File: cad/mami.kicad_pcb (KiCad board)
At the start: 2 copper layers, 258.4 x 86.7 mm, 128 parts, among them SW1 SW_Push, SW10 SW_Push, SW11 SW_Push, SW12 SW_Push, SW13 SW_Push, SW14 SW_Push, SW15 SW_Push, SW16 SW_Push, SW17 SW_Push, SW18 SW_Push, SW19 SW_Push, SW2 SW_Push, SW20 SW_Push, SW21 SW_Push, SW22 SW_Push, SW23 SW_Push, SW24 SW_Push, SW25 SW_Push, SW26 SW_Push, SW27 SW_Push, SW28 SW_Push, SW29 SW_Push, SW3 SW_Push, SW30 SW_Push, SW31 SW_Push, SW32 SW_Push, SW33 SW_Push, SW34 SW_Push, SW35 SW_Push, SW36 SW_Push, SW37 SW_Push, SW38 SW_Push, SW39 SW_Push, SW4 SW_Push, SW40 SW_Push, SW41 SW_Push, SW42 SW_Push, SW43 ResetSW, SW5 SW_Push, SW6 SW_Push, SW7 SW_Push, SW8 SW_Push, SW9 SW_Push

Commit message: ON/OFFスイッチを削除
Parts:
- removed REF**: SuperMini, taku:nano
- added U1: nice_nano, salicylic-3:Micon_KMC_7sKB, F.Cu at (150.2, 62.9)
- moved D77 244.7 mm to (265.2, 100.0)
- moved D78 243.8 mm to (269.4, 80.9)
- moved D79 237.6 mm to (267.3, 61.9)
- moved D76 227.9 mm to (246.2, 99.9)
- moved D66 227.5 mm to (228.6, 118.4), turned to 8 degrees
- moved D75 225.8 mm to (248.1, 80.9)
- moved D80 217.8 mm to (248.1, 62.0)
- moved D67 216.4 mm to (225.9, 99.4), turned to 8 degrees
- moved D65 211.9 mm to (207.4, 121.2), turned to 8 degrees
- moved D74 207.5 mm to (228.1, 79.9), turned to 8 degrees
- moved D68 197.8 mm to (207.0, 102.1), turned to 8 degrees
- moved D81 196.2 mm to (227.4, 60.9), turned to 8 degrees
- moved D73 191.9 mm to (209.2, 82.5), turned to 8 degrees
- moved D64 190.5 mm to (176.8, 125.5), turned to 8 degrees
- moved D69 179.3 mm to (188.1, 104.7), turned to 8 degrees
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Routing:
- net col5: track 3.03 -> 0.49 mm, vias 3 -> 2
- net VCC: track 1.99 -> 0.00 mm, vias 1 -> 0
- net GND: track 1.41 -> 0.00 mm
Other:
- board size 258.4 x 86.7 mm -> 258.4 x 87.9 mm

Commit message: reverse diode direction
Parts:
- SW1, SW10, SW11, SW12, SW13, SW15, SW16, SW17, SW18, SW19, SW2, SW20, SW22, SW23, SW24, SW26, SW27, SW28, SW29, SW3, SW30, SW31, SW33, SW34, SW35, SW36, SW37, SW38, SW39, SW4, SW40, SW41, SW42, SW5, SW6, SW7, SW8, SW9: footprint kbd:keyswitch_cherrymx_hotswap_1u -> kbd-sw:CherryMX_Hotswap_1u
- SW14, SW32: footprint kbd:keyswitch_cherrymx_hotswap_1u -> kbd-sw:CherryMX_Hotswap_1.25u
- SW21, SW25: footprint kbd:keyswitch_cherrymx_hotswap_1u -> kbd-sw:CherryMX_Hotswap_2u
- U1: value nice_nano -> Micon_BLEMicroPro; footprint salicylic-3:Micon_KMC_7sKB -> kbd-parts:Micon_BMP_7sKB; moved to B.Cu
- moved D14 14.9 mm to (101.9, 123.9), turned to 82 degrees
- moved D40 14.7 mm to (274.6, 63.3), turned to 90 degrees
- moved D27 14.7 mm to (197.8, 85.5), turned to 98 degrees
- moved D30 14.6 mm to (216.7, 82.7), turned to 98 degrees
- moved D22 14.6 mm to (178.4, 69.1), turned to 98 degrees
- moved D32 14.5 mm to (215.1, 121.3), turned to 98 degrees
- moved D33 14.5 mm to (234.8, 61.1), turned to 98 degrees
- moved D29 14.5 mm to (216.1, 63.8), turned to 98 degrees
- moved D39 14.5 mm to (253.4, 101.3), turned to 90 degrees
- moved D13 14.5 mm to (100.4, 104.4), turned to 82 degrees
- moved D25 14.5 mm to (184.0, 125.9), turned to 98 degrees
- moved D21 14.5 mm to (131.1, 127.7), turned to 82 degrees
- moved D20 14.5 mm to (138.2, 109.7), turned to 82 degrees
- moved D9 14.5 mm to (81.8, 101.8), turned to 82 degrees
- moved D26 14.5 mm to (197.1, 66.3), turned to 98 degrees
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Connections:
- U1 pad 25: (no net) -> BAT+
- U1 pad 26: (no net) -> GND
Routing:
- net row0: track 1.27 -> 0.00 mm
- net Net-(D15-A): track 0.00 -> 1.27 mm
- net col5: track 0.49 -> 0.00 mm, vias 2 -> 0

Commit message: pcb枠を修正
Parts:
- moved SW43 18.9 mm to (150.1, 64.8)
- moved U1 10.8 mm to (150.2, 74.3)
- moved SW2 2.45 mm to (33.3, 76.2)
- moved D2 2.45 mm to (40.9, 81.8)
- moved D49 2.45 mm to (33.3, 80.9)
- moved D78 2.27 mm to (267.2, 81.0)
- moved D41 2.27 mm to (274.4, 82.1)
- moved SW41 2.27 mm to (267.2, 76.2)
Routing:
- net Net-(D15-A): track 1.27 -> 0.00 mm
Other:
- board size 258.4 x 87.9 mm -> 253.1 x 87.4 mm

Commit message: 自動配線
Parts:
- added J1: Conn_01x02_Pin, kbd-parts:Battery_BMP_2pin, B.Cu at (161.6, 70.2)
- SW43: moved to B.Cu
- moved SW43 28.6 mm to (122.8, 73.2), turned to -8 degrees
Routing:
- net VCC: track 0.00 -> 1027.1 mm, vias 0 -> 82
- net GND: track 0.00 -> 1018.7 mm, vias 0 -> 72
- net col0: track 0.00 -> 342.0 mm, vias 0 -> 9
- net col1: track 0.00 -> 286.1 mm, vias 0 -> 8
- net col2: track 0.00 -> 283.6 mm, vias 0 -> 6
- net col3: track 0.00 -> 241.2 mm, vias 0 -> 5
- net col4: track 0.00 -> 166.0 mm, vias 0 -> 2
- net col5: track 0.00 -> 163.4 mm, vias 0 -> 3
- net row6: track 0.00 -> 140.6 mm, vias 0 -> 4
- net row2: track 0.00 -> 135.8 mm, vias 0 -> 3
- net row4: track 0.00 -> 133.4 mm, vias 0 -> 9
- net row5: track 0.00 -> 128.2 mm, vias 0 -> 3
- net row7: track 0.00 -> 123.8 mm, vias 0 -> 5
- net row0: track 0.00 -> 117.0 mm, vias 0 -> 9
- net row1: track 0.00 -> 116.5 mm, vias 0 -> 1
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
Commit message: routing width > 0.250mm
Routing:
- net GND: track 1018.7 -> 994.8 mm, vias 72 -> 67
- net col4: track 166.0 -> 181.6 mm, vias 2 -> 7
- net Net-(D60-DOUT): track 30.6 -> 44.1 mm, vias 2 -> 6
- net Net-(D83-DOUT): track 28.6 -> 41.3 mm, vias 2 -> 4
- net Net-(D49-DOUT): track 22.8 -> 35.2 mm, vias 2 -> 4
- net Net-(D46-DOUT): track 30.8 -> 40.9 mm, vias 2 -> 4
- net Net-(D75-DOUT): track 28.5 -> 37.6 mm, vias 2 -> 4
- net VCC: track 1027.1 -> 1018.2 mm, vias 82 -> 81
- net col3: track 241.2 -> 249.5 mm
- net Net-(D44-DOUT): track 34.1 -> 42.3 mm, vias 2 -> 4
- net Net-(D57-DOUT): track 50.3 -> 42.2 mm, vias 6 -> 4
- net col0: track 342.0 -> 334.6 mm, vias 9 -> 3
- net Net-(D43-DOUT): track 38.7 -> 45.5 mm
- net row4: track 133.4 -> 139.9 mm, vias 9 -> 11
- net Net-(D80-DOUT): track 47.0 -> 40.8 mm, vias 6 -> 4
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
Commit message: ラベリング
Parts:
- J1: moved to F.Cu
- turned J1 to 180 degrees
- renumbered SW5 to A, SW20 to B, SW39 to BLSH, SW40 to BSPC, SW13 to C, SW32 to CMD, SW14 to CMD, SW38 to COLON, SW31 to COMMA, SW10 to CTRL, SW12 to D, D83 to D41, SW35 to DOT, SW11 to E, SW1 to ECS, SW41 to ENTER, SW16 to F, SW19 to G, SW23 to H, SW29 to I, SW27 to J, SW30 to K, SW34 to L, D43 to L1, D52 to L10, D53 to L11, D54 to L12, D55 to L13, D56 to L14, D57 to L15, D58 to L16, D59 to L17, D60 to L18, D61 to L19, D44 to L2, D62 to L20, D63 to L21, D64 to L22, D65 to L23, D66 to L24, D67 to L25, D68 to L26, D69 to L27, D70 to L28, D71 to L29, D45 to L3, D72 to L30, D73 to L31, D74 to L32, D75 to L33, D76 to L34, D77 to L35, D78 to L36, D79 to L37, D80 to L38, D81 to L39, D46 to L4, D82 to L40, D84 to L42, D47 to L5, D48 to L6, D49 to L7, D50 to L8, D51 to L9, SW28 to M, SW24 to N, SW33 to O, SW36 to OPT, SW37 to P, SW4 to Q, SW15 to R, SW8 to S, SW3 to SHIFT, SW42 to SHIFT, SW25 to SPACE, SW21 to SPACE, SW18 to T, SW2 to TAB, SW26 to U, SW17 to V, SW7 to W, SW9 to X, SW22 to Y, SW6 to Z
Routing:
- net row7: track 117.8 -> 181.1 mm, vias 6 -> 4
- net VCC: track 1018.2 -> 1006.4 mm, vias 81 -> 91
- net col3: track 249.5 -> 261.1 mm, vias 5 -> 4
- net Net-(D57-DOUT): track 42.2 -> 33.0 mm, vias 4 -> 2
- net col2: track 282.9 -> 291.6 mm, vias 8 -> 10
- net Net-(D34-A): track 11.7 -> 20.1 mm, vias 1 -> 3
- net col1: track 292.1 -> 283.9 mm, vias 3 -> 5
- net Net-(D82-DOUT): track 38.8 -> 30.7 mm, vias 6 -> 4
- net row0: track 119.8 -> 111.8 mm, vias 2 -> 1
- net row2: track 130.7 -> 138.6 mm, vias 3 -> 5
- net GND: track 994.8 -> 987.2 mm, vias 67 -> 66
- net Net-(D44-DOUT): track 42.3 -> 49.3 mm, vias 4 -> 6
- net Net-(D59-DOUT): track 46.8 -> 39.8 mm
- net Net-(D67-DOUT): track 34.0 -> 40.9 mm, vias 8 -> 4
- net row5: track 132.4 -> 139.1 mm, vias 5 -> 6
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
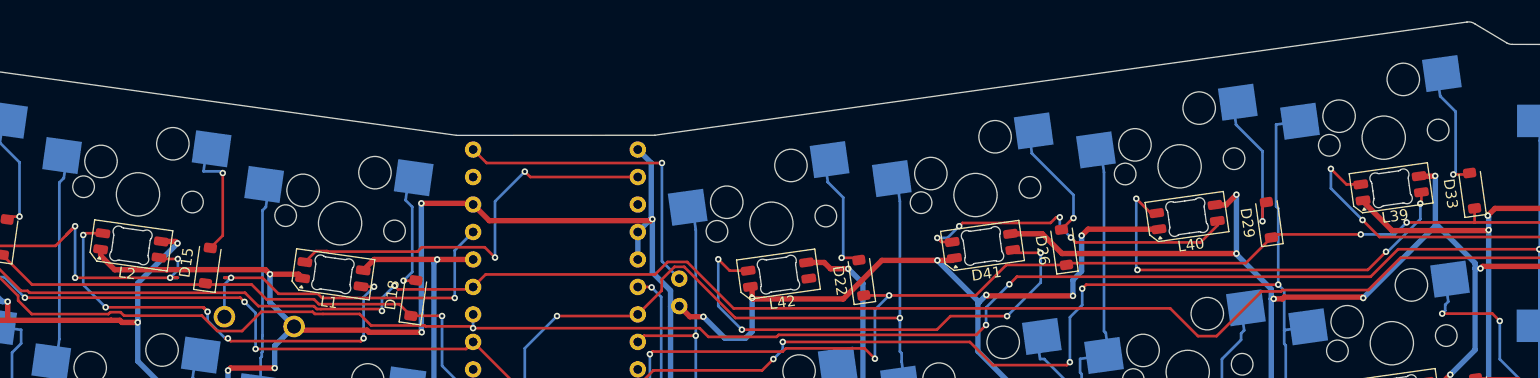
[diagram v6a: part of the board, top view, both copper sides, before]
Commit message: 自動配線エラーを修正
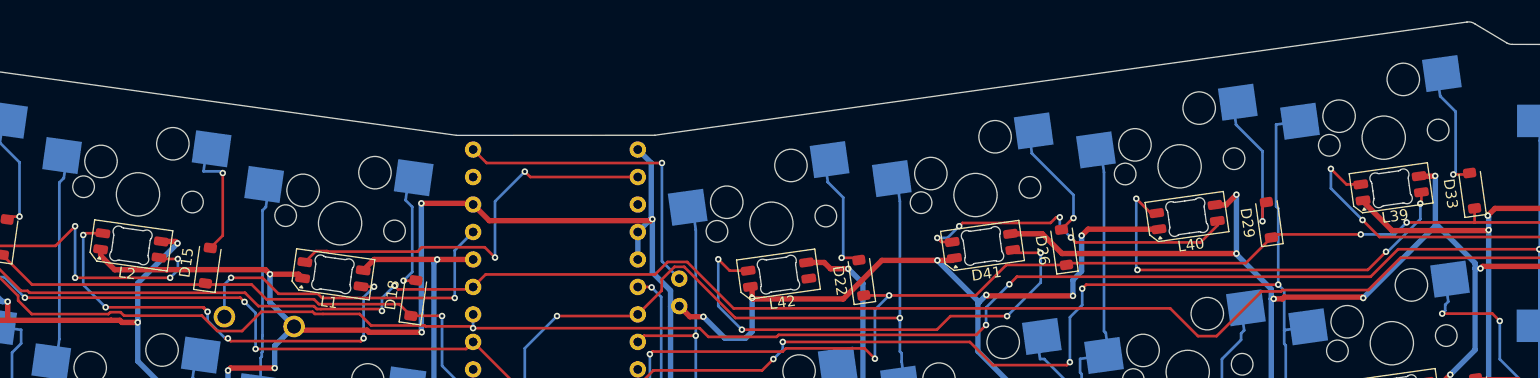
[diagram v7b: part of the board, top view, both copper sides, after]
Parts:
- renumbered COMMA to ,
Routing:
- net Net-(D44-DOUT): track 49.3 -> 41.9 mm
- net reset: track 34.6 -> 32.1 mm
- net Net-(D43-DOUT): track 46.3 -> 45.1 mm
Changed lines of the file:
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@@
 		(layer "F.Cu")
 		(at 206.3375 97.375 8)
-		(property "Reference" "COMMA"
+		(property "Reference" ","
 			(at 0 8 8)
 			(layer "B.SilkS")
@@
 	(gr_arc
 		(start 234.376625 45.485216)
-		(mid 234.754232 45.497722)
+		(mid 234.754237 45.49771)
 		(end 235.1 45.65)
 		(stroke
@@
 	)
 	(segment
-		(start 114.5171 69.1228)
-		(end 115.2293 69.1228)
-		(width 0.25)
-		(layer "F.Cu")
-		(net "Net-(D44-DOUT)")
-	)
-	(segment
 		(start 103.9147 66.1746)
 		(end 105.7334 64.3559)
@@
 	)
 	(segment
-		(start 104.9161 65.1732)
-		(end 105.7334 64.3559)
-		(width 0.25)
-		(layer "F.Cu")
-		(net "Net-(D44-DOUT)")
-	)
-	(segment
 		(start 90.6771 66.3456)
 		(end 90.8481 66.1746)
@@
 	)
 	(segment
-		(start 105.7334 64.3559)
-		(end 104.9161 65.1732)
-		(width 0.25)
-		(layer "F.Cu")
-		(net "Net-(D44-DOUT)")
-	)
-	(segment
-		(start 115.2293 69.1228)
-		(end 114.5171 69.1228)
-		(width 0.25)
-		(layer "F.Cu")
-		(net "Net-(D44-DOUT)")
-	)
-	(segment
 		(start 115.2293 67.3799)
 		(end 113.6143 67.3799)
@@
 	)
 	(segment
-		(start 105.7334 64.3559)
-		(end 104.9161 65.1732)
-		(width 0.25)
-		(layer "B.Cu")
-		(net "Net-(D44-DOUT)")
-	)
-	(segment
 		(start 115.2293 68.4106)
 		(end 115.2293 67.3799)
@@
 	)
 	(segment
-		(start 115.2293 69.1228)
-		(end 114.5171 69.1228)
-		(width 0.25)
-		(layer "B.Cu")
-		(net "Net-(D44-DOUT)")
-	)
-	(segment
-		(start 114.5171 69.1228)
-		(end 115.2293 69.1228)
-		(width 0.25)
-		(layer "B.Cu")
-		(net "Net-(D44-DOUT)")
-	)
-	(segment
-		(start 104.9161 65.1732)
-		(end 105.7334 64.3559)
-		(width 0.25)
-		(layer "B.Cu")
-		(net "Net-(D44-DOUT)")
-	)
-	(segment
 		(start 105.7334 64.3559)
 		(end 105.7334 69.1228)
@@
 	)
 	(segment
-		(start 117.5673 71.8515)
-		(end 117.9748 72.259)
-		(width 0.25)
-		(layer "B.Cu")
-		(net "Net-(D43-DOUT)")
-	)
-	(segment
 		(start 132.3971 70.9192)
 		(end 132.3971 74.7156)
@@
 	)
 	(segment
-		(start 117.9748 72.259)
-		(end 117.5673 71.8515)
-		(width 0.25)
-		(layer "B.Cu")
-		(net "Net-(D43-DOUT)")
-	)
-	(segment
 		(start 119.6177 74.7233)
 		(end 119.8591 74.7233)
@@
 	)
 	(segment
-		(start 119.5316 69.1228)
-		(end 120.1491 69.1228)
-		(width 0.25)
-		(layer "F.Cu")
-		(net "reset")
-	)
-	(segment
-		(start 120.1491 69.1228)
-		(end 119.5316 69.1228)
-		(width 0.25)
-		(layer "F.Cu")
-		(net "reset")
-	)
-	(segment
 		(start 128.1758 70.6051)
 		(end 124.5414 70.6051)
@@
 		(net "reset")
 	)
-	(segment
-		(start 120.1491 69.1228)
-		(end 119.5316 69.1228)
-		(width 0.25)
-		(layer "B.Cu")
-		(net "reset")
-	)
-	(segment
-		(start 119.5316 69.1228)
-		(end 120.1491 69.1228)
-		(width 0.25)
-		(layer "B.Cu")
-		(net "reset")
-	)

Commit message: 署名を追加
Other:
- board text added: "Authored by t.mori"
- board text added: "Mami42 v1.0"
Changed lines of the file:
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@@
 		(layer "User.2")
+	)
+	(gr_text "Mami42 v1.0"
+		(at 155 128 0)
+		(layer "B.SilkS")
+		(effects
+			(font
+				(size 1 1)
+				(thickness 0.1)
+			)
+			(justify left bottom mirror)
+		)
+	)
+	(gr_text "Authored by t.mori"
+		(at 157 130.5 0)
+		(layer "B.SilkS")
+		(effects
+			(font
+				(size 1 1)
+				(thickness 0.1)
+			)
+			(justify left bottom mirror)
+		)
 	)
 	(segment
